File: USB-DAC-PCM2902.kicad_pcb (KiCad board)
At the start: 2 copper layers, 75 x 50 mm, 25 parts, among them J1 Conn_01x02, J2 PJ-320D, U1 USB_PCB, U2 PCM2902, U3 LP2951CM, Y1 O12M

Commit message: update vol button,
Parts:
- added SW1: MUTE, Button_Switch_THT:SW_PUSH_6mm_H4.3mm, F.Cu at (41.5, 9.16)
- added SW2: VOL_DOWN, Button_Switch_THT:SW_PUSH_6mm_H4.3mm, F.Cu at (33.6, 9.16)
- added SW3: VOL_UP, Button_Switch_THT:SW_PUSH_6mm_H4.3mm, F.Cu at (25.7, 9.16)
- moved R3 10.8 mm to (27.1, 20.3)
- moved R1 7.16 mm to (35.5, 21.0)
- moved R2 6.90 mm to (30.7, 18.1)
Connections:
- U2 pad 28: Net-(U2-Pad28) -> /PIN28
- U2 pad 5: Net-(U2-Pad5) -> /VOL_MUTE
- U2 pad 6: Net-(U2-Pad6) -> /VOL_DOWN
- U2 pad 7: Net-(U2-Pad7) -> /VOL_UP
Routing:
- net /PIN28: track 0.00 -> 51.8 mm
- net /VOL_UP: track 0.00 -> 34.3 mm
- net /VOL_DOWN: track 0.00 -> 27.1 mm
- net /VOL_MUTE: track 0.00 -> 23.2 mm
- net Net-(R3-Pad1): track 10.9 -> 22.1 mm
- net Net-(R3-Pad2): track 33.1 -> 23.5 mm
- net Net-(R1-Pad2): track 41.9 -> 34.5 mm
- net Net-(C1-Pad1): track 32.4 -> 39.6 mm
- net Net-(R2-Pad1): track 8.51 -> 15.6 mm

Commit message: update,
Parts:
- moved C1 13.0 mm to (67.0, 14.7), turned to 180 degrees
- moved J2 11.6 mm to (62.9, 27.8)
- moved C8 10.4 mm to (66.8, 36.5), turned to 90 degrees
- moved C11 10.3 mm to (61.2, 36.5), turned to 90 degrees
- moved C6 8.98 mm to (67.0, 20.1), turned to 180 degrees
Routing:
- net Net-(C8-Pad1): track 11.7 -> 29.0 mm
- net Net-(C11-Pad1): track 5.01 -> 20.2 mm
- net /OUTL: track 16.5 -> 3.92 mm
- net /OUTR: track 17.6 -> 5.01 mm
- net GND: track 157.2 -> 152.7 mm, vias 3 -> 4
- net Net-(C6-Pad1): track 24.7 -> 21.9 mm
- net Net-(C1-Pad1): track 39.6 -> 41.7 mm, vias 4 -> 2

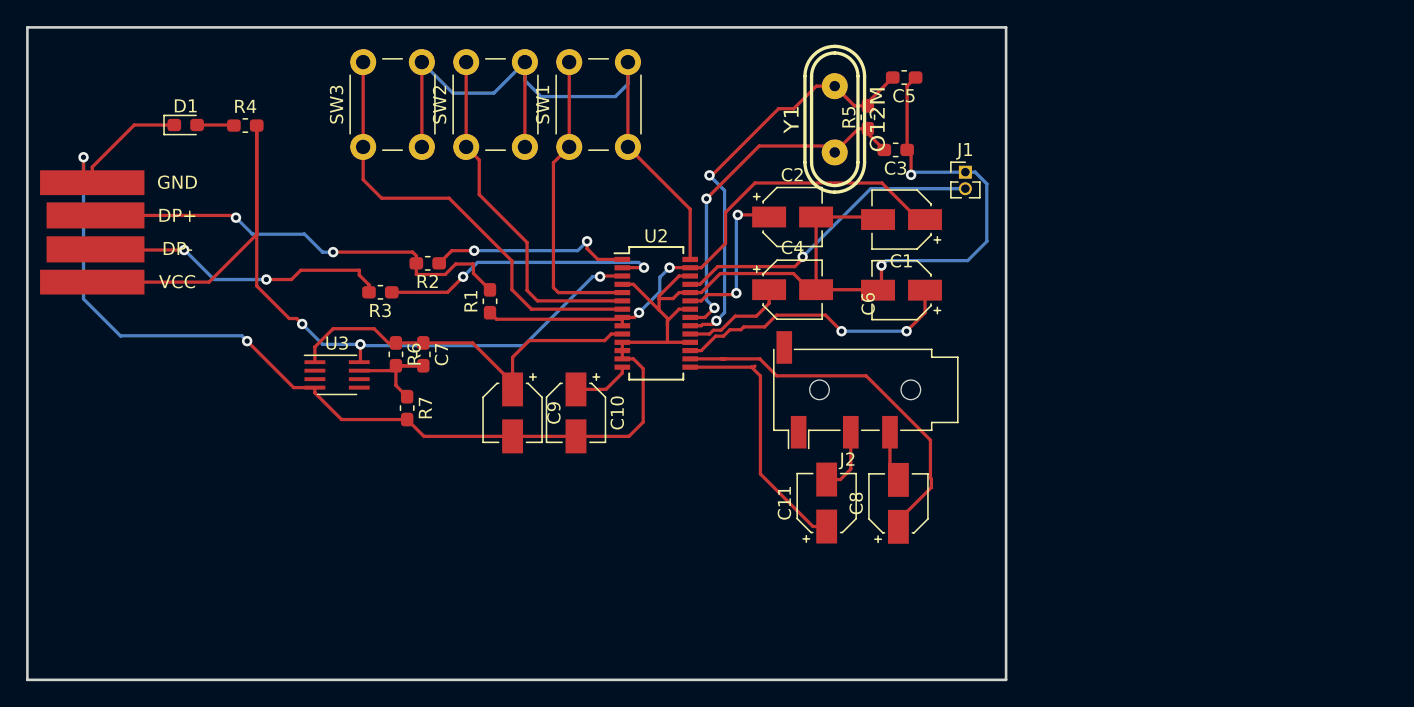
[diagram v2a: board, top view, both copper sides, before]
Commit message: reduce vias,
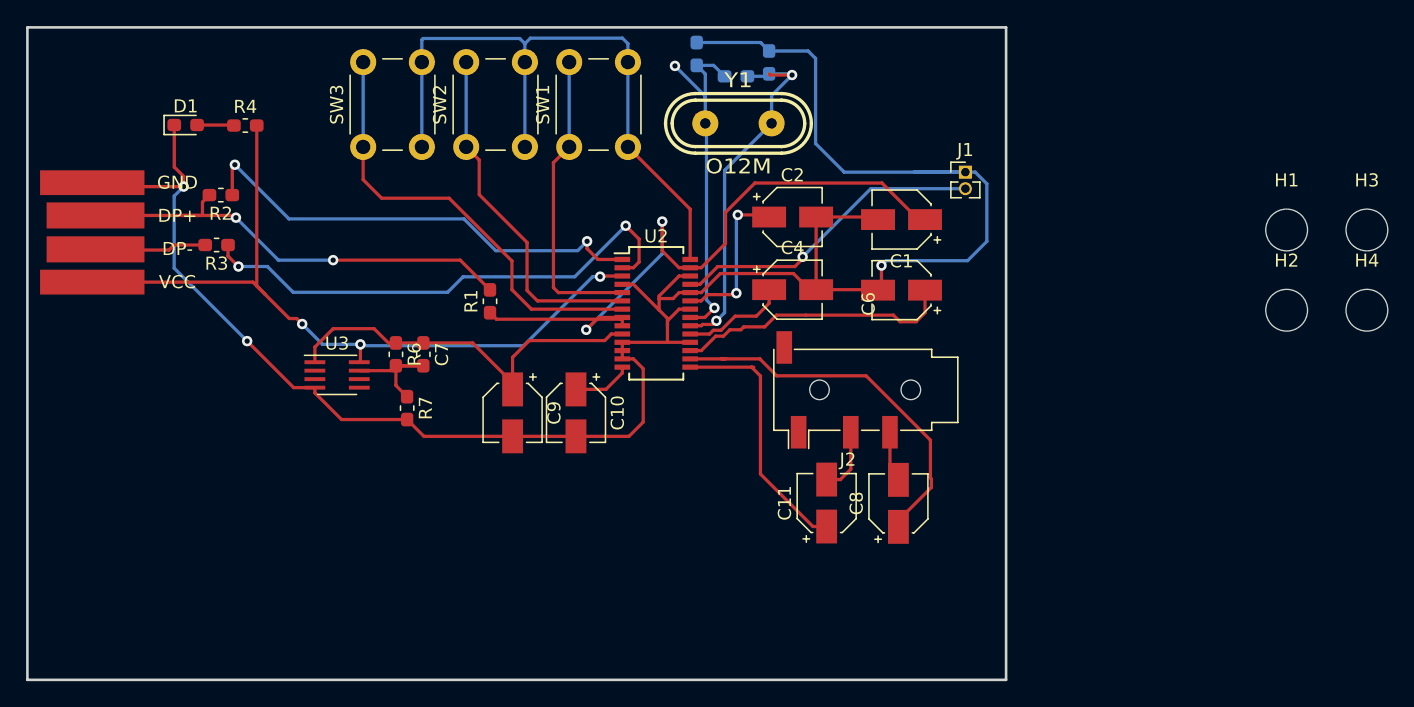
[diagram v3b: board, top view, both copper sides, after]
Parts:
- added H1: MOUNT_M3, MountingHole:MountingHole_3.2mm_M3_DIN965, F.Cu at (96.5, 15.5)
- added H2: MOUNT_M3, MountingHole:MountingHole_3.2mm_M3_DIN965, F.Cu at (96.5, 21.7)
- added H3: MOUNT_M3, MountingHole:MountingHole_3.2mm_M3_DIN965, F.Cu at (102.7, 15.5)
- added H4: MOUNT_M3, MountingHole:MountingHole_3.2mm_M3_DIN965, F.Cu at (102.7, 21.7)
- C3, C5, R5: moved to B.Cu
- moved R2 16.7 mm to (14.8, 12.8)
- moved C5 16.0 mm to (51.3, 2.04), turned to 270 degrees
- moved R3 13.1 mm to (14.5, 16.7)
- moved C3 11.8 mm to (56.8, 2.69), turned to 270 degrees
- moved R5 10.6 mm to (54.3, 3.75), turned to 0 degrees
- moved Y1 7.39 mm to (54.5, 7.36), turned to 0 degrees
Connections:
- R5 pad 1: Net-(C3-Pad2) -> Net-(C5-Pad2)
- R5 pad 2: Net-(C5-Pad2) -> Net-(C3-Pad2)
- U2 pad 20: Net-(C5-Pad2) -> Net-(C3-Pad2)
- U2 pad 21: Net-(C3-Pad2) -> Net-(C5-Pad2)
- Y1 pad 1: Net-(C3-Pad2) -> Net-(C5-Pad2)
- Y1 pad 2: Net-(C5-Pad2) -> Net-(C3-Pad2)
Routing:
- net Net-(R2-Pad1): track 15.6 -> 36.0 mm
- net Net-(R3-Pad1): track 22.1 -> 39.3 mm
- net Net-(R3-Pad2): track 23.5 -> 8.59 mm, vias 2 -> 0
- net Net-(C1-Pad1): track 41.7 -> 53.1 mm
- net GND: track 152.7 -> 162.3 mm, vias 4 -> 3
- net Net-(R4-Pad2): track 68.3 -> 59.4 mm
- net Net-(C5-Pad2): track 33.2 -> 28.0 mm
- net Net-(R1-Pad2): track 34.5 -> 35.8 mm
- net /PIN28: track 51.8 -> 51.0 mm
- net Net-(C3-Pad2): track 28.1 -> 28.7 mm
- net Net-(C6-Pad1): track 21.9 -> 21.3 mm, vias 2 -> 0

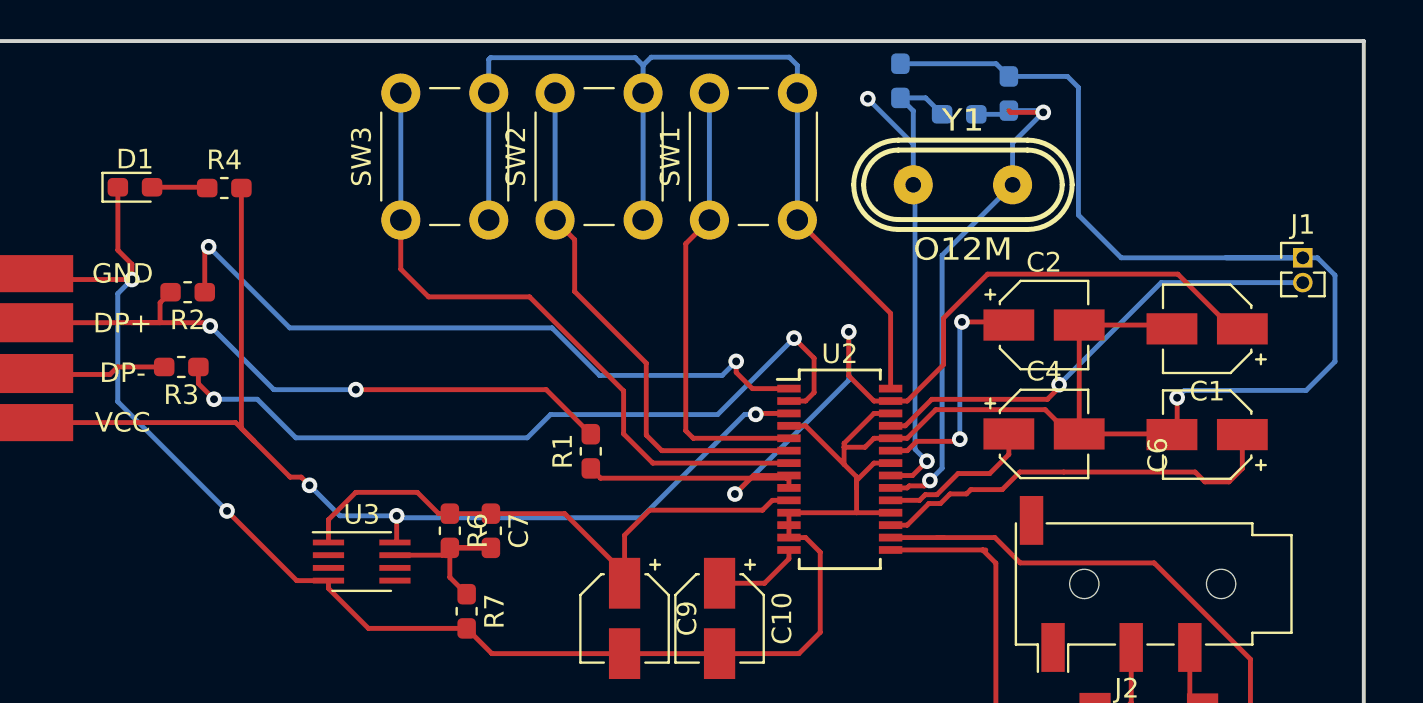
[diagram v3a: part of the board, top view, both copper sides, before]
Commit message: make vias 1.5mm,
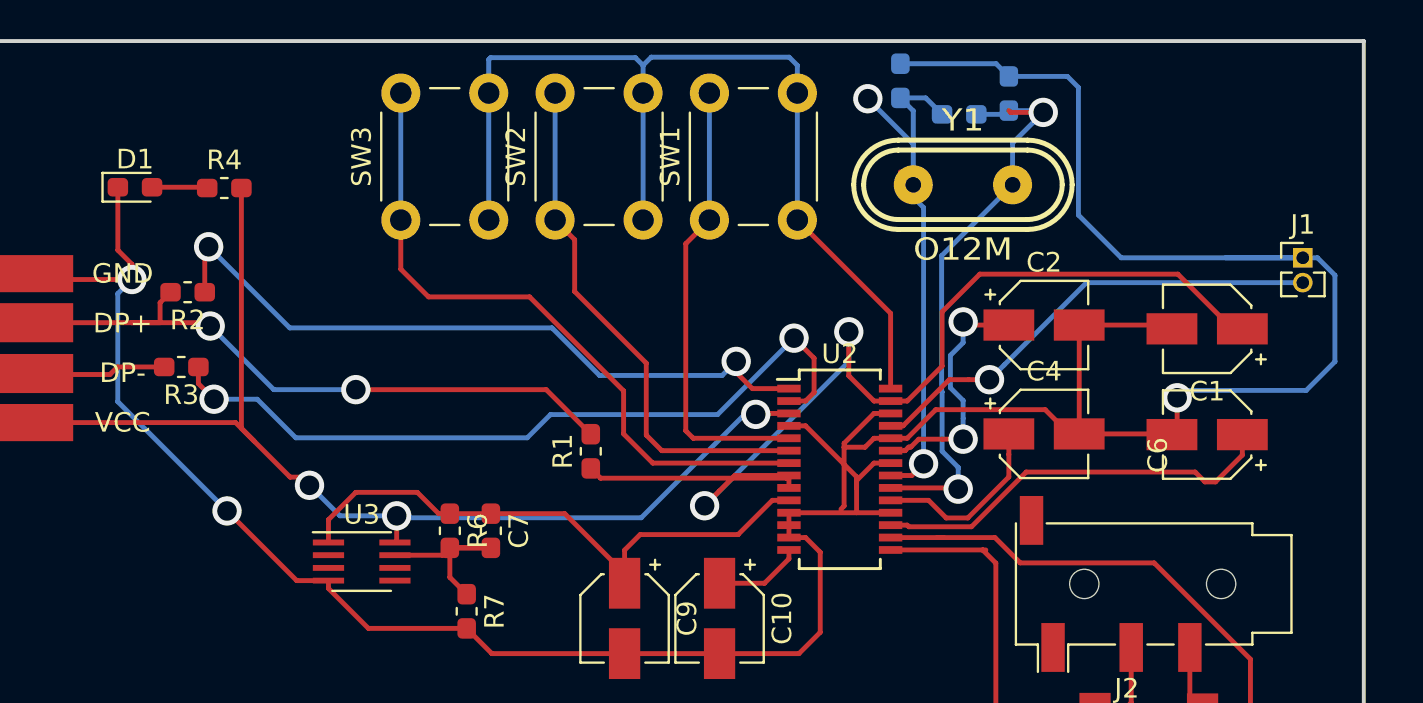
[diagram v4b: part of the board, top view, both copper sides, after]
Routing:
- net Net-(C1-Pad1): track 53.1 -> 56.3 mm
- net GND: track 162.3 -> 164.7 mm
- net Net-(C3-Pad2): track 28.7 -> 30.6 mm
- net Net-(C4-Pad1): track 8.57 -> 9.99 mm
- net Net-(C2-Pad1): track 12.3 -> 12.9 mm

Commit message: draft ok,
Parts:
- moved R1 13.8 mm to (21.8, 19.1)
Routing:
- net Net-(C1-Pad1): track 56.3 -> 73.9 mm
- net Net-(R1-Pad2): track 35.8 -> 22.2 mm
- net GND: track 164.7 -> 174.6 mm
- net Net-(C3-Pad2): track 30.6 -> 26.5 mm, vias 2 -> 1
- net /VOL_MUTE: track 23.2 -> 26.8 mm
- net /VOL_UP: track 34.3 -> 37.7 mm
- net /VOL_DOWN: track 27.1 -> 29.1 mm
- net Net-(R4-Pad2): track 59.4 -> 61.3 mm
- net Net-(R3-Pad1): track 39.3 -> 40.7 mm
- net /PIN28: track 51.0 -> 51.8 mm

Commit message: draft ok,
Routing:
- net Net-(C5-Pad2): track 27.8 -> 24.3 mm, vias 2 -> 1
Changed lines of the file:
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@@
     (thickness 1.6)
     (drawings 4)
-    (tracks 308)
+    (tracks 304)
     (zones 0)
     (modules 32)
@@
   (gr_line (start 0 50) (end 75 50) (layer Edge.Cuts) (width 0.2))
   (gr_line (start 0 0) (end 0 50) (layer Edge.Cuts) (width 0.2))
-  (via (at 49.625 2.95) (size 1.5) (drill 1) (layers F.Cu B.Cu) (net 2))
-  (segment (start 51.95 5.275) (end 49.625 2.95) (width 0.25) (layer B.Cu) (net 2))
   (segment (start 51.56 7.745) (end 51.95 7.355001) (width 0.25) (layer F.Cu) (net 2) (status 30))
   (segment (start 51.29 6.695001) (end 51.95 7.355001) (width 0.25) (layer F.Cu) (net 2) (status 30))
@@
   (segment (start 56.84 7.165) (end 57.03 7.355) (width 0.25) (layer B.Cu) (net 1))
   (segment (start 56.84 3.56) (end 56.84 7.165) (width 0.25) (layer B.Cu) (net 1))
-  (segment (start 49.665 2.91) (end 49.625 2.95) (width 0.25) (layer F.Cu) (net 2))
   (segment (start 51.95 3.57) (end 51.29 2.91) (width 0.25) (layer B.Cu) (net 2) (status 20))
   (segment (start 51.95 5.4) (end 51.95 3.57) (width 0.25) (layer B.Cu) (net 2))
   (segment (start 51.95 7.355) (end 51.95 5.4) (width 0.25) (layer B.Cu) (net 2) (status 10))
-  (segment (start 51.95 5.4) (end 51.95 5.275) (width 0.25) (layer B.Cu) (net 2))
   (segment (start 52.584999 2.91) (end 53.425 3.750001) (width 0.25) (layer B.Cu) (net 2) (status 20))
   (segment (start 51.29 2.91) (end 52.584999 2.91) (width 0.25) (layer B.Cu) (net 2) (status 10))

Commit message: draft ok,
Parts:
- moved J1 10.9 mm to (65.3, 2.38), turned to 270 degrees
- moved C1 1.00 mm to (68.0, 14.7)
- moved C2 1.00 mm to (59.6, 14.5)
- moved C4 1.00 mm to (59.6, 20.1)
- moved C6 1.00 mm to (68.0, 20.1)
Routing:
- net GND: track 174.6 -> 168.6 mm
- net Net-(C1-Pad1): track 73.9 -> 76.1 mm
- net Net-(C3-Pad2): track 26.5 -> 27.2 mm
- net Net-(C2-Pad1): track 12.9 -> 13.5 mm

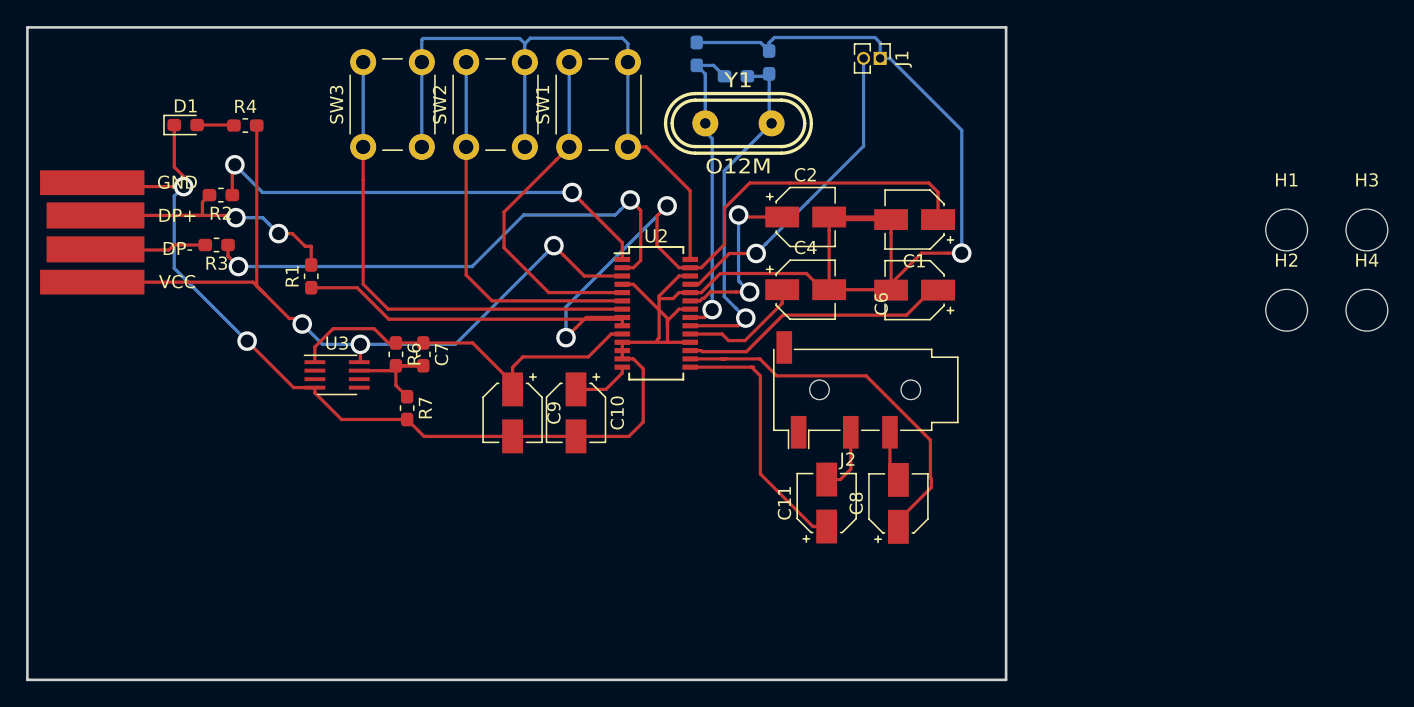
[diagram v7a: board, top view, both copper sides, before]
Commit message: upadte pcb shape,
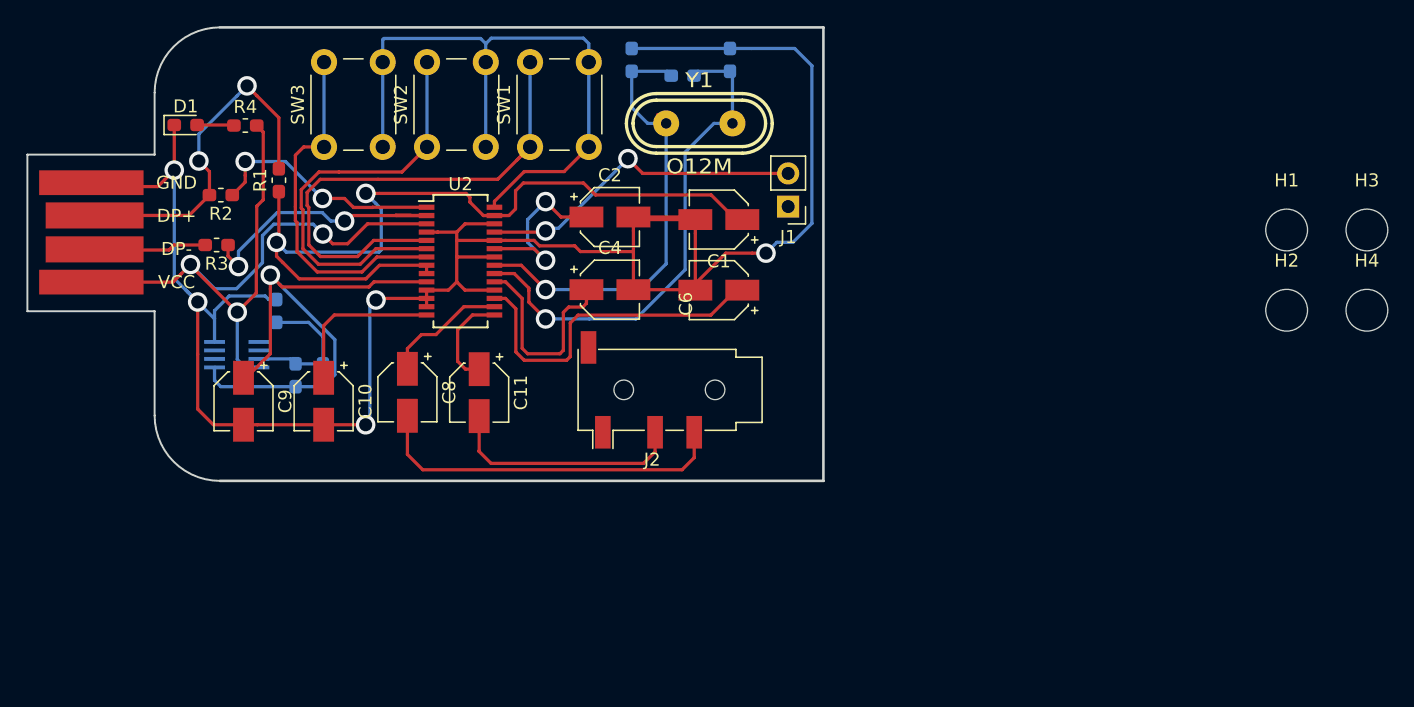
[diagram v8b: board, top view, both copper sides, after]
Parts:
- C7, R6, R7, U3: moved to B.Cu
- J1: footprint Connector_PinHeader_1.27mm:PinHeader_1x02_P1.27mm_Vertical -> Connector_PinHeader_2.54mm:PinHeader_1x02_P2.54mm_Vertical
- moved C8 38.6 mm to (29.1, 28.0), turned to 270 degrees
- moved C11 27.9 mm to (34.6, 28.0), turned to 270 degrees
- moved C9 20.6 mm to (16.6, 28.6)
- moved C10 19.4 mm to (22.7, 28.6)
- moved U2 15.5 mm to (33.2, 17.9)
- moved C1 15.0 mm to (53.0, 14.7)
- moved C2 15.0 mm to (44.6, 14.5)
- moved C4 15.0 mm to (44.6, 20.1)
- moved C6 15.0 mm to (53.0, 20.1)
- moved J2 15.0 mm to (47.9, 27.8)
- moved J1 13.4 mm to (58.3, 13.7), turned to 180 degrees
- moved R7 12.5 mm to (19.1, 21.7), turned to 90 degrees
- moved C7 7.85 mm to (22.6, 26.7), turned to 90 degrees
- moved R6 7.85 mm to (20.6, 26.7), turned to 90 degrees
- moved U3 7.84 mm to (16.0, 25.1)
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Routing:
- net /OUTL: track 3.92 -> 27.8 mm
- net Net-(C8-Pad1): track 29.0 -> 9.55 mm
- net Net-(R3-Pad1): track 40.7 -> 22.8 mm
- net Net-(R2-Pad1): track 35.9 -> 18.3 mm
- net /VOL_MUTE: track 26.8 -> 40.4 mm
- net /OUTR: track 5.01 -> 18.5 mm
- net Net-(C11-Pad1): track 20.1 -> 7.16 mm
- net Net-(C1-Pad1): track 76.1 -> 64.3 mm
- net Net-(C5-Pad2): track 24.3 -> 36.1 mm
- net Net-(C7-Pad1): track 30.3 -> 41.9 mm, vias 0 -> 1
- net Net-(C3-Pad2): track 27.2 -> 38.8 mm
- net /VOL_UP: track 37.7 -> 27.4 mm
- net Net-(C10-Pad1): track 4.52 -> 12.2 mm
- net Net-(C4-Pad1): track 9.99 -> 16.4 mm
- net GND: track 168.6 -> 162.8 mm, vias 3 -> 5
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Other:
- board size 75 x 50 mm -> 61 x 34.8 mm
